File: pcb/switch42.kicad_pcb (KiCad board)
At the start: 2 copper layers, 114.3 x 81 mm, 84 parts, among them J1 MJ-4PP-9, J2 Conn_01x03, SW1 SW_PUSH, SW10 SW_PUSH, SW11 SW_PUSH, SW12 SW_PUSH, SW13 SW_PUSH, SW14 SW_PUSH, SW15 SW_PUSH, SW16 SW_PUSH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

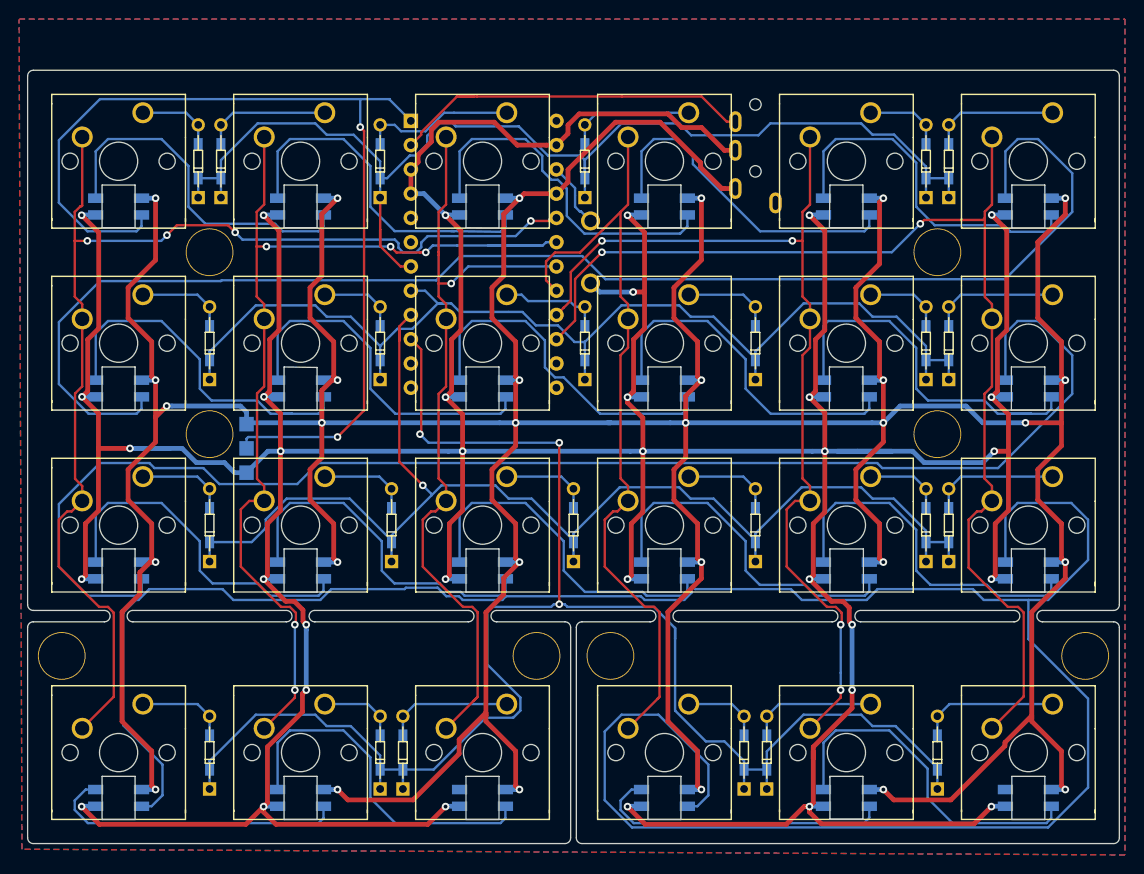
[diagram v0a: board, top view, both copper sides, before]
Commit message: Add jumpers to use underglow alongside backlights / update footprints
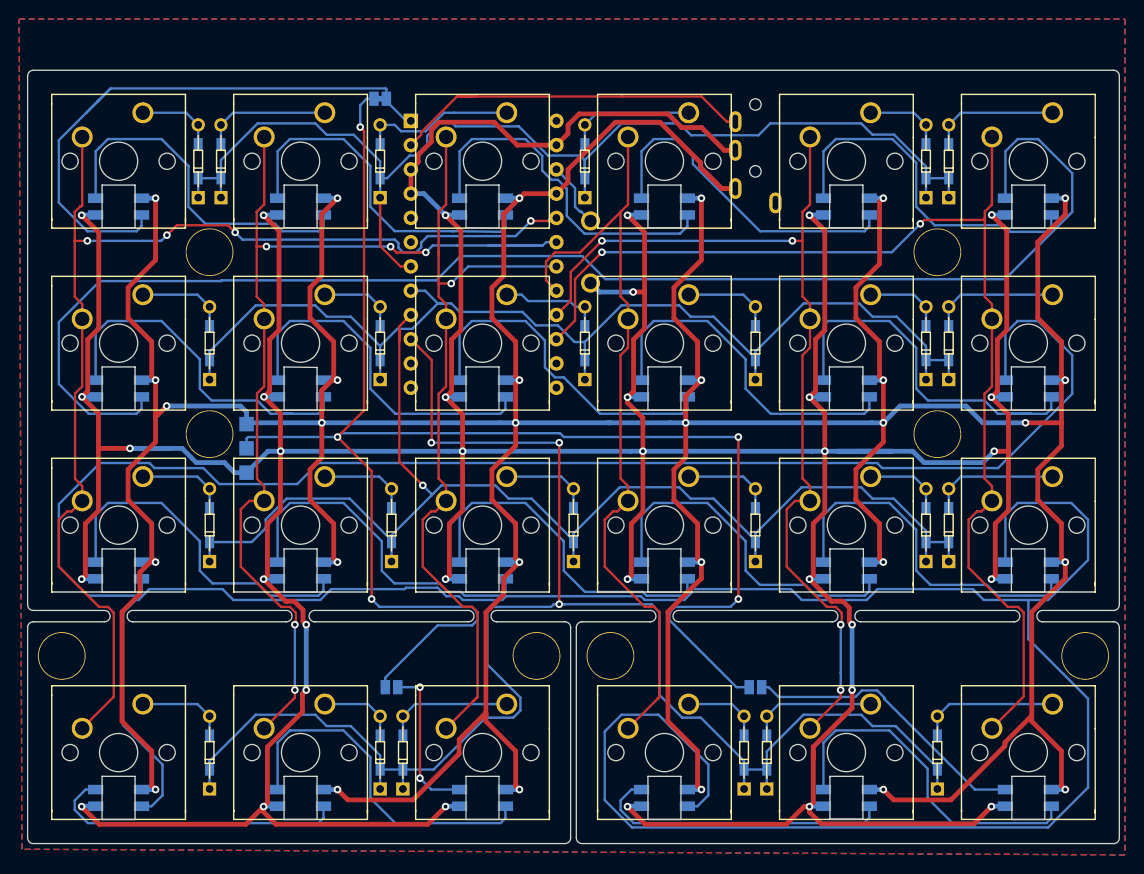
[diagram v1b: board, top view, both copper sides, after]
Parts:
- added JP1: Jumper, phi-kbd-library:Jumper-Closed, B.Cu at (88.1, 38.0)
- added JP2: Jumper_NO_Small, phi-kbd-library:Jumper-Open, B.Cu at (89.3, 99.6)
- added JP3: Jumper_NO_Small, phi-kbd-library:Jumper-Open, B.Cu at (127.4, 99.6)
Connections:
- J2 pad 2: led -> underglow
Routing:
- net underglow: track 0.00 -> 171.6 mm, vias 0 -> 5
- net led: track 104.5 -> 63.1 mm, vias 2 -> 0
- net Net-(JP3-Pad1): track 0.00 -> 30.6 mm
- net Net-(JP2-Pad1): track 0.00 -> 16.5 mm, vias 0 -> 2
- net row3: track 175.1 -> 174.1 mm
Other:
- board text added: "* switch42 v0.4 designed by @zk_phi *"
- board text removed: "* switch42 v0.3 designed by @zk_phi *"

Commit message: Add slide sw to toggle LEDs
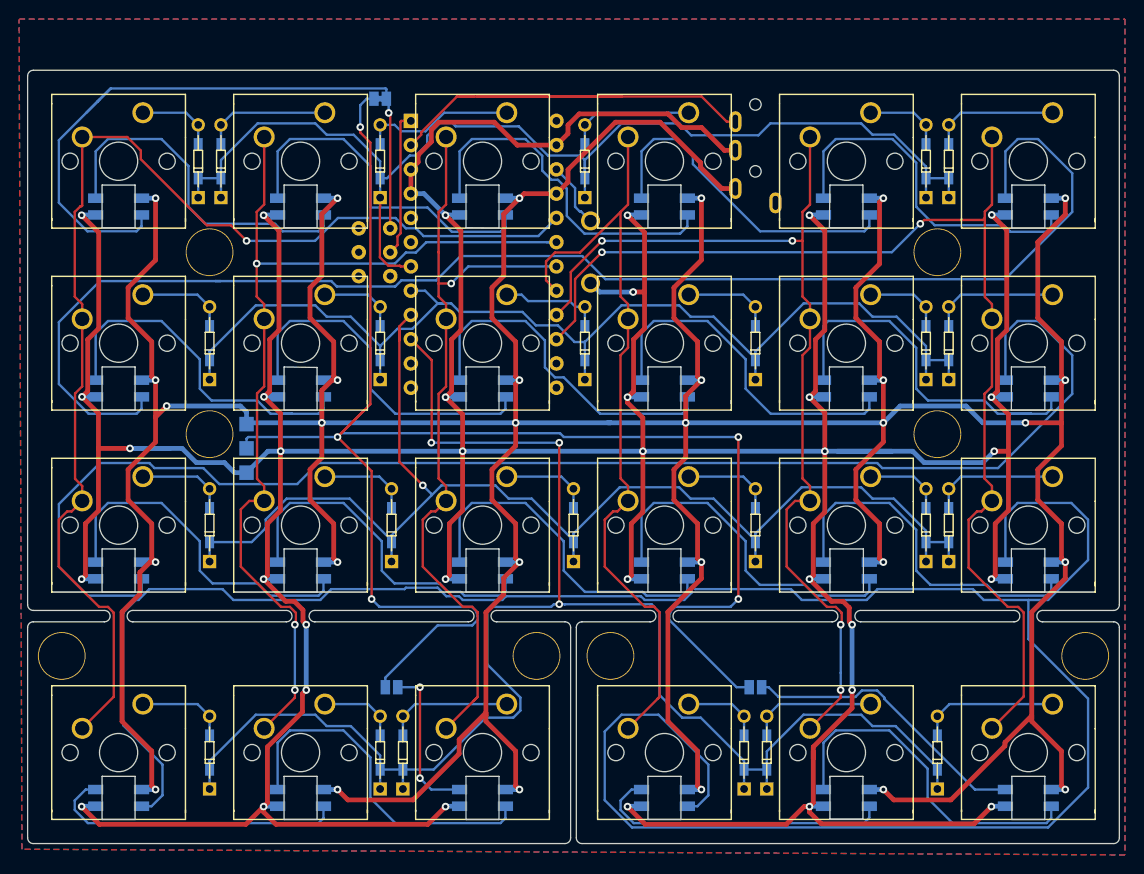
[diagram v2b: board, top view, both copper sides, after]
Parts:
- added SW26: SW_DPDT_x2, phi-kbd-library:IS-2235-irreversible, B.Cu at (87.5, 54.1)
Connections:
- U1 pad 1: led -> Net-(SW26-Pad2)
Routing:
- net Net-(SW26-Pad2): track 0.00 -> 15.7 mm
- net data: track 38.9 -> 54.0 mm
- net led: track 63.1 -> 73.4 mm, vias 0 -> 1
- net col1: track 107.5 -> 102.8 mm, vias 5 -> 3
- net underglow: track 171.6 -> 176.0 mm
- net col0: track 123.2 -> 126.5 mm, vias 4 -> 1
- net Net-(L2-Pad3): track 148.7 -> 149.8 mm
- net row0: track 122.5 -> 121.6 mm

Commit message: Control VCC with the slide sw, instead of LED signals
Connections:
- J2 pad 1: VCC -> ledpower
- L1 pad 4: VCC -> ledpower
- L10 pad 4: VCC -> ledpower
- L11 pad 4: VCC -> ledpower
- L12 pad 4: VCC -> ledpower
- L13 pad 4: VCC -> ledpower
- L14 pad 4: VCC -> ledpower
- L15 pad 4: VCC -> ledpower
- L16 pad 4: VCC -> ledpower
- L17 pad 4: VCC -> ledpower
- L18 pad 4: VCC -> ledpower
- L19 pad 4: VCC -> ledpower
- L2 pad 4: VCC -> ledpower
- L20 pad 4: VCC -> ledpower
- L21 pad 4: VCC -> ledpower
- L22 pad 4: VCC -> ledpower
- L23 pad 4: VCC -> ledpower
- L24 pad 4: VCC -> ledpower
- L3 pad 4: VCC -> ledpower
- L4 pad 4: VCC -> ledpower
- L5 pad 4: VCC -> ledpower
- L6 pad 4: VCC -> ledpower
- L7 pad 4: VCC -> ledpower
- L8 pad 4: VCC -> ledpower
- L9 pad 4: VCC -> ledpower
- SW26 pad 2: Net-(SW26-Pad2) -> VCC
- SW26 pad 3: led -> ledpower
- U1 pad 1: Net-(SW26-Pad2) -> led
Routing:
- net ledpower: track 0.00 -> 547.8 mm, vias 0 -> 31
- net VCC: track 569.6 -> 47.8 mm, vias 30 -> 2
- net Net-(SW26-Pad2): track 15.7 -> 0.00 mm
- net led: track 73.4 -> 64.1 mm, vias 1 -> 0
